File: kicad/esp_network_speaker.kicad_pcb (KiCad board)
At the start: 2 copper layers, 13 parts, among them U1 ESP12, U2 23A1024, U3 PCM5100A

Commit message: kicad project updated
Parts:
- added C11: 100nF, Capacitors_SMD:C_0603_HandSoldering, F.Cu at (114.3, 104.1)
- added C12: 100nF, Capacitors_SMD:C_0603_HandSoldering, F.Cu at (99.1, 95.2)
- added R1: 470, Resistors_SMD:R_0603_HandSoldering, F.Cu at (110.5, 101.6)
- added R2: 470, Resistors_SMD:R_0603_HandSoldering, F.Cu at (101.6, 100.3)
- added R3: 10k, Resistors_SMD:R_0603_HandSoldering, F.Cu at (106.7, 104.1)
- U1: value ESP12 -> 23LC1024; footprint ESP12:ESP12 -> Housings_SOIC:SOIC-8_3.9x4.9mm_Pitch1.27mm
- U2: value 23A1024 -> ESP12; footprint SMD_Packages:SOIC-8-N -> ESP12:ESP12
- moved U1 53.5 mm to (106.7, 95.2)
- moved C9 38.3 mm to (105.4, 106.7)
- moved C7 37.0 mm to (106.7, 109.2)
- moved U2 7.18 mm to (115.6, 105.4)
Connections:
- U1 pad 1: (no net) -> ESP12_CS
- U1 pad 2: (no net) -> ESP12_MISO
- U1 pad 4: (no net) -> GND
- U1 pad 5: (no net) -> ESP12_MOSI
- U1 pad 6: (no net) -> ESP12_CLK
- U1 pad 7: (no net) -> +3V3
- U1 pad 8: (no net) -> +3V3
- U2 pad 5: (no net) -> ESP12_CLK
- U2 pad 6: (no net) -> ESP12_MISO
- U2 pad 7: (no net) -> ESP12_MOSI
- U2 pad 8: (no net) -> +3V3
- U3 pad 12: (no net) -> GND
- U3 pad 13: (no net) -> DAC_BCK
- U3 pad 14: (no net) -> DAC_DATA
- U3 pad 15: (no net) -> DAC_LRCK
- U3 pad 6: (no net) -> DAC_OUTL
- U3 pad 7: (no net) -> DAC_OUTR
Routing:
- net +3V3: track 5.77 -> 0.00 mm
- net GND: track 6.26 -> 0.63 mm
- net Net-(C10-Pad2): track 5.52 -> 0.32 mm
- net Net-(C6-Pad2): track 4.12 -> 0.00 mm
- net Net-(C10-Pad1): track 3.45 -> 0.00 mm

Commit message: wip, most of the components are in now
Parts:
- added D1: LED, Resistors_SMD:R_0603_HandSoldering, F.Cu at (129.3, 74.4)
- added D2: LED, Resistors_SMD:R_0603_HandSoldering, F.Cu at (125.2, 67.8)
- added R4: 220, Resistors_SMD:R_0603_HandSoldering, F.Cu at (94.7, 60.7)
- added R5: 220, Resistors_SMD:R_0603_HandSoldering, F.Cu at (102.9, 68.3)
- added R6: 1k, Resistors_SMD:R_0603_HandSoldering, F.Cu at (112.5, 64.8)
- added R7: 1k, Resistors_SMD:R_0603_HandSoldering, F.Cu at (109.0, 70.9)
- added R8: 1k, Resistors_SMD:R_0603_HandSoldering, F.Cu at (113.5, 82.5)
- added R9: 1k, Resistors_SMD:R_0603_HandSoldering, F.Cu at (115.6, 69.8)
- added SW1: SW_PUSH, Buttons_Switches_SMD:SW_SPST_FSMSM, F.Cu at (112.0, 76.5)
- added U4: TSR_1-2433, TSR-1, F.Cu at (101.3, 81.5)
- U2: footprint ESP12:ESP12 -> ESP12
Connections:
- U2 pad 19: (no net) -> LEDA
- U2 pad 20: (no net) -> LEDB
- U2 pad 3: (no net) -> Net-(R9-Pad1)

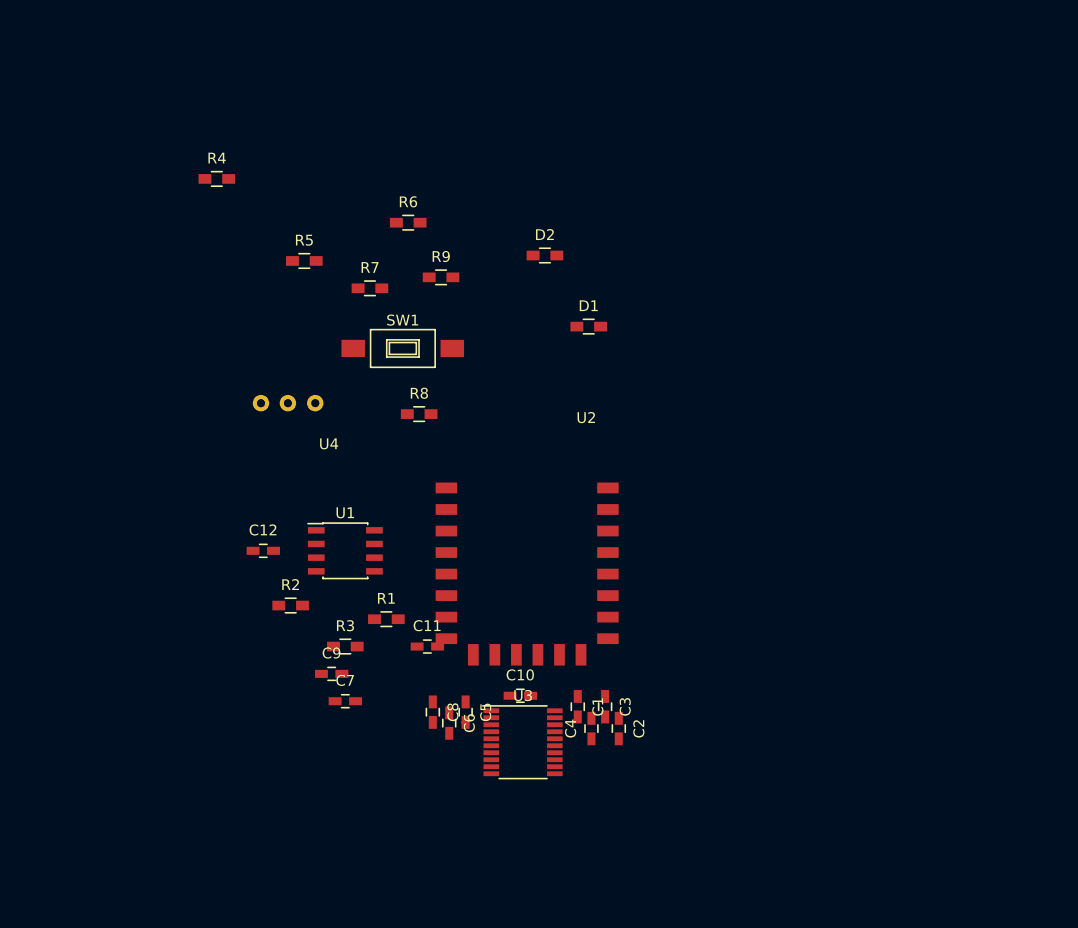
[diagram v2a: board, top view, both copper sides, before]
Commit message: schematic finished, some placement done
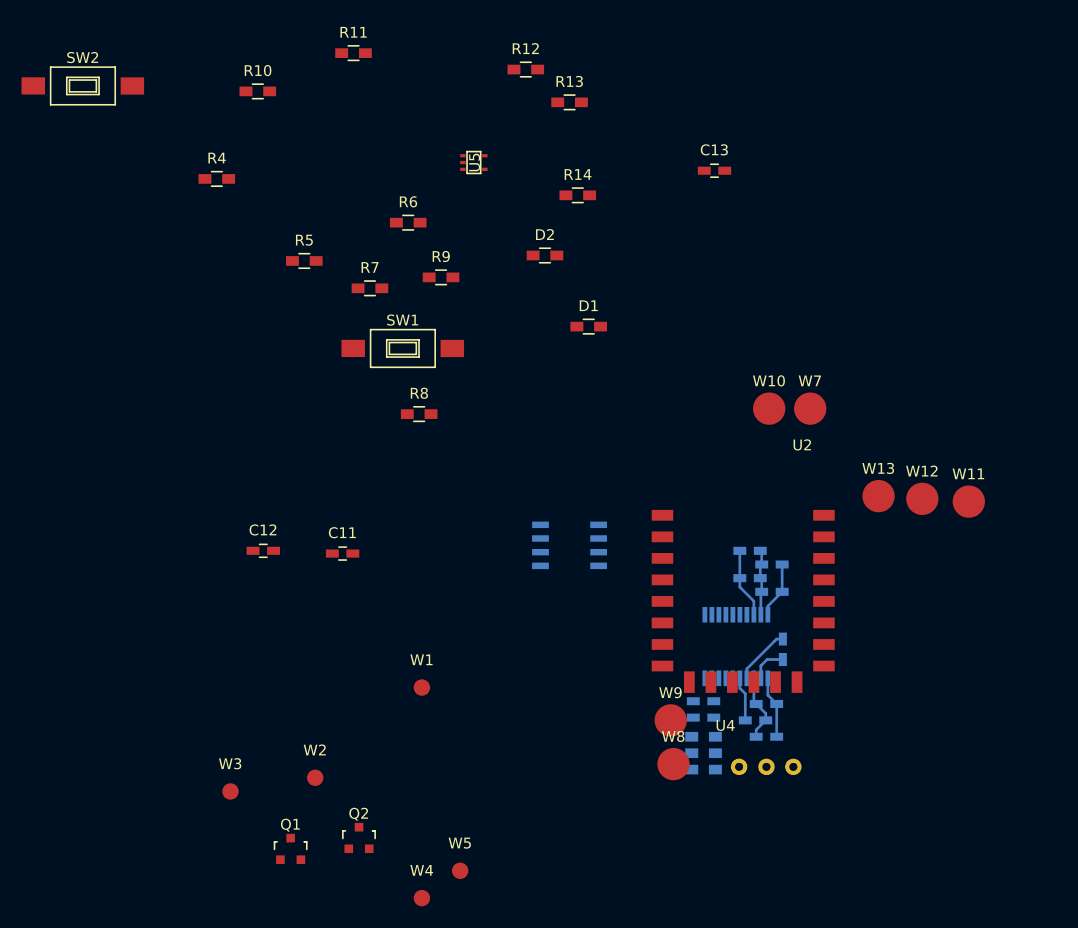
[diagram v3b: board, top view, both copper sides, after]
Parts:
- added C13: 100nF, Capacitors_SMD:C_0603_HandSoldering, F.Cu at (141.0, 59.9)
- added Q1: Q_NPN_BEC, TO_SOT_Packages_SMD:SOT-23, F.Cu at (101.6, 122.9)
- added Q2: Q_NPN_BEC, TO_SOT_Packages_SMD:SOT-23, F.Cu at (108.0, 121.9)
- added R10: 1k, Resistors_SMD:R_0603_HandSoldering, F.Cu at (98.6, 52.6)
- added R11: 100, Resistors_SMD:R_0603_HandSoldering, F.Cu at (107.4, 49.0)
- added R12: 1k, Resistors_SMD:R_0603_HandSoldering, F.Cu at (123.4, 50.5)
- added R13: 10k, Resistors_SMD:R_0603_HandSoldering, F.Cu at (127.5, 53.6)
- added R14: 10k, Resistors_SMD:R_0603_HandSoldering, F.Cu at (128.3, 62.2)
- added SW2: SW_PUSH, Buttons_Switches_SMD:SW_SPST_FSMSM, F.Cu at (82.3, 52.1)
- added U5: M74VHC1GT125, TO_SOT_Packages_SMD:SOT-353, F.Cu at (118.6, 59.2)
- added W1: TEST_1P, Measurement_Points:Measurement_Point_Round-SMD-Pad_Small, F.Cu at (113.8, 108.0)
- added W10: PGND, Measurement_Points:Measurement_Point_Round-SMD-Pad_Big, F.Cu at (146.1, 82.0)
- added W11: PROG_GND, Measurement_Points:Measurement_Point_Round-SMD-Pad_Big, F.Cu at (164.6, 90.7)
- added W12: PROG_RX, Measurement_Points:Measurement_Point_Round-SMD-Pad_Big, F.Cu at (160.3, 90.4)
- added W13: PROG_TX, Measurement_Points:Measurement_Point_Round-SMD-Pad_Big, F.Cu at (156.2, 90.2)
- added W2: TEST_1P, Measurement_Points:Measurement_Point_Round-SMD-Pad_Small, F.Cu at (103.9, 116.3)
- added W3: TEST_1P, Measurement_Points:Measurement_Point_Round-SMD-Pad_Small, F.Cu at (96.0, 117.6)
- added W4: TEST_1P, Measurement_Points:Measurement_Point_Round-SMD-Pad_Small, F.Cu at (113.8, 127.5)
- added W5: TEST_1P, Measurement_Points:Measurement_Point_Round-SMD-Pad_Small, F.Cu at (117.3, 125.0)
- added W7: AOUT, Measurement_Points:Measurement_Point_Round-SMD-Pad_Big, F.Cu at (149.9, 82.0)
- added W8: AGND, Measurement_Points:Measurement_Point_Round-SMD-Pad_Big, F.Cu at (137.2, 115.1)
- added W9: PBATT, Measurement_Points:Measurement_Point_Round-SMD-Pad_Big, F.Cu at (136.9, 111.0)
- C1, C10, C2, C3, C4, C5, C6, C7, C8, C9, R1, R2, R3, U1, U3: moved to B.Cu
- R6, R7, R8, R9: value 1k -> 10k
- U2: footprint ESP12 -> ESP12:ESP12
- U4: footprint TSR-1 -> traco:TSR-1
- moved U4 55.8 mm to (145.8, 115.3), turned to 180 degrees
- moved R2 40.2 mm to (140.0, 112.5)
- moved R3 35.2 mm to (140.0, 115.6)
- moved C9 34.6 mm to (140.0, 109.2), turned to 180 degrees
- moved C7 33.3 mm to (140.0, 110.7), turned to 180 degrees
- moved R1 32.0 mm to (140.0, 114.0)
- moved C8 31.1 mm to (145.8, 112.5), turned to 180 degrees
- moved C6 28.4 mm to (144.8, 111.0), turned to 180 degrees
- moved C5 28.0 mm to (145.8, 109.5), turned to 180 degrees
- moved C10 24.8 mm to (147.3, 104.4), turned to 90 degrees
- moved U3 21.7 mm to (143.0, 104.1), turned to 90 degrees
- moved C1 21.0 mm to (146.3, 99.1), turned to 180 degrees
- moved U1 20.8 mm to (127.5, 94.7), turned to 180 degrees
- moved C2 20.5 mm to (144.3, 95.2), turned to 180 degrees
- moved C3 20.4 mm to (146.3, 96.5), turned to 180 degrees
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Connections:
- net DAC_OUTM renamed Net-(R1-Pad1)
- SW1 pad 1: DAC_BCK -> +3V3
- SW1 pad 2: GND -> Net-(R10-Pad2)
- U2 pad 1: (no net) -> ESP12_RESET
- U2 pad 16: DAC_BCK -> Net-(R11-Pad2)
- U2 pad 22: (no net) -> ESP12_TX
- U3 pad 17: (no net) -> DAC_MUTE
- U4 pad 1: (no net) -> /VBATT
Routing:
- net GND: track 0.63 -> 12.7 mm
- net +3V3: track 0.00 -> 11.0 mm
- net Net-(C2-Pad2): track 0.00 -> 6.48 mm
- net Net-(C10-Pad2): track 0.32 -> 5.69 mm
- net Net-(C6-Pad2): track 0.00 -> 4.12 mm
- net Net-(C10-Pad1): track 0.00 -> 3.45 mm

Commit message: routing in progress, first pass almost finished
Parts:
- C11, C13, Q1, Q2, R10, R12, R13, R14, R8, R9, U5, W1, W2, W3, W4, W5: moved to B.Cu
- moved SW2 73.5 mm to (132.6, 105.7), turned to 90 degrees
- moved R11 72.4 mm to (153.4, 105.0), turned to 90 degrees
- moved R4 63.6 mm to (153.7, 84.6), turned to 270 degrees
- moved R10 62.2 mm to (132.6, 104.6), turned to 180 degrees
- moved R6 59.4 mm to (152.1, 109.0)
- moved R5 55.3 mm to (155.7, 84.6), turned to 270 degrees
- moved R12 53.1 mm to (132.5, 102.9), turned to 180 degrees
- moved R7 52.9 mm to (153.4, 99.6), turned to 270 degrees
- moved W3 51.5 mm to (146.8, 109.0)
- moved W2 45.8 mm to (149.1, 109.0)
- moved R13 44.5 mm to (132.4, 97.8)
- moved C12 40.1 mm to (136.4, 110.0), turned to 270 degrees
- moved W4 38.3 mm to (148.3, 111.0)
- moved D2 36.9 mm to (155.7, 88.6), turned to 270 degrees
- moved Q1 35.0 mm to (132.8, 107.2), turned to 270 degrees
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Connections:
- U2 pad 11: (no net) -> DAC_MUTE
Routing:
- net GND: track 12.7 -> 121.9 mm, vias 0 -> 2
- net +3V3: track 11.0 -> 54.2 mm, vias 0 -> 2
- net DAC_BCK: track 0.00 -> 39.0 mm, vias 0 -> 2
- net ESP12_RESET: track 0.00 -> 22.9 mm, vias 0 -> 1
- net ESP12_CS: track 0.00 -> 21.6 mm, vias 0 -> 3
- net DAC_DATA: track 0.00 -> 21.0 mm, vias 0 -> 1
- net /PROG_EN: track 0.00 -> 20.8 mm
- net Net-(R10-Pad2): track 0.00 -> 19.1 mm, vias 0 -> 1
- net ESP12_MISO: track 0.00 -> 17.9 mm, vias 0 -> 1
- net DAC_LRCK: track 0.00 -> 17.3 mm, vias 0 -> 1
- net ESP12_MOSI: track 0.00 -> 16.8 mm, vias 0 -> 1
- net DAC_MUTE: track 0.00 -> 15.9 mm, vias 0 -> 1
- net Net-(R1-Pad1): track 0.00 -> 14.1 mm, vias 0 -> 1
- net ESP12_CLK: track 0.00 -> 13.9 mm, vias 0 -> 1
- net /VBATT: track 0.00 -> 12.1 mm
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
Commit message: wip
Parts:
- R4, R5, R6: moved to B.Cu
- moved W9 14.2 mm to (151.5, 113.8)
- moved R5 12.2 mm to (153.4, 96.5), turned to 90 degrees
- moved D2 8.20 mm to (153.4, 96.5)
- moved R4 6.36 mm to (153.4, 90.9), turned to 90 degrees
- moved R6 2.90 mm to (150.4, 106.7), turned to 180 degrees
- moved U4 2.69 mm to (143.3, 114.4)
- moved D1 2.30 mm to (153.4, 90.9)
- moved W12 2.27 mm to (142.5, 82.0)
- moved W7 2.17 mm to (151.6, 82.0)
- moved W13 2.13 mm to (139.1, 82.0)
- moved W10 2.07 mm to (148.2, 82.0)
- moved W11 2.05 mm to (135.6, 82.0)
- moved W8 1.40 mm to (133.3, 113.9)
- moved R7 1.14 mm to (153.4, 100.7)
- moved U5 0.63 mm to (132.3, 87.8)
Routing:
- net +3V3: track 54.2 -> 126.4 mm, vias 2 -> 6
- net GND: track 121.9 -> 179.1 mm, vias 2 -> 11
- net DAC_DATA: track 21.0 -> 42.6 mm, vias 1 -> 2
- net ESP12_TX: track 0.00 -> 13.5 mm
- net /PROG_TX: track 0.00 -> 10.3 mm, vias 0 -> 1
- net LEDA: track 11.2 -> 2.43 mm
- net /VBATT: track 12.1 -> 6.02 mm
- net LEDB: track 7.58 -> 4.93 mm
- net Net-(R1-Pad1): track 14.1 -> 11.9 mm
- net Net-(D2-Pad1): track 1.86 -> 3.05 mm, vias 0 -> 1
- net DAC_LRCK: track 17.3 -> 16.2 mm
- net DAC_MUTE: track 15.9 -> 16.9 mm
- net Net-(D1-Pad1): track 1.86 -> 2.63 mm, vias 0 -> 1
- net Net-(R10-Pad2): track 19.1 -> 19.6 mm
- added copper zone on F.Cu, net /VBATT
- added copper zone on B.Cu, net GND
- added copper zone on F.Cu, net GND
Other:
- net class Default: trace_width 0.25 -> 0.2
- net class n added: clearance 0.2, trace_width 0.4, via_dia 0.6, via_drill 0.4

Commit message: wip, gerber files generated for rev A
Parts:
- renumbered W2 to BCK, W4 to DTA, W3 to LRK, W5 to MTE, W1 to PRGEN
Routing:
- net (no net): track 0.00 -> 3.17 mm
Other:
- board outline added: 24.1 x 36.3 mm
- board text added: "A"
- board text added: "ESP12 NETWORK SPEAKER"
- board text added: "GND"
- board text added: "RX"
- board text added: "TX"
- board text added: "VIN"
- board text added: "https://github.com/JDRobotter/esp8266_network_speaker"
